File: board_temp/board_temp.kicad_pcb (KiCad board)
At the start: 2 copper layers, 4 parts, among them J1 Conn_02x16_Odd_Even, J2 Battery input, U1 BQ24074RGT, U2 INA219AxDCN

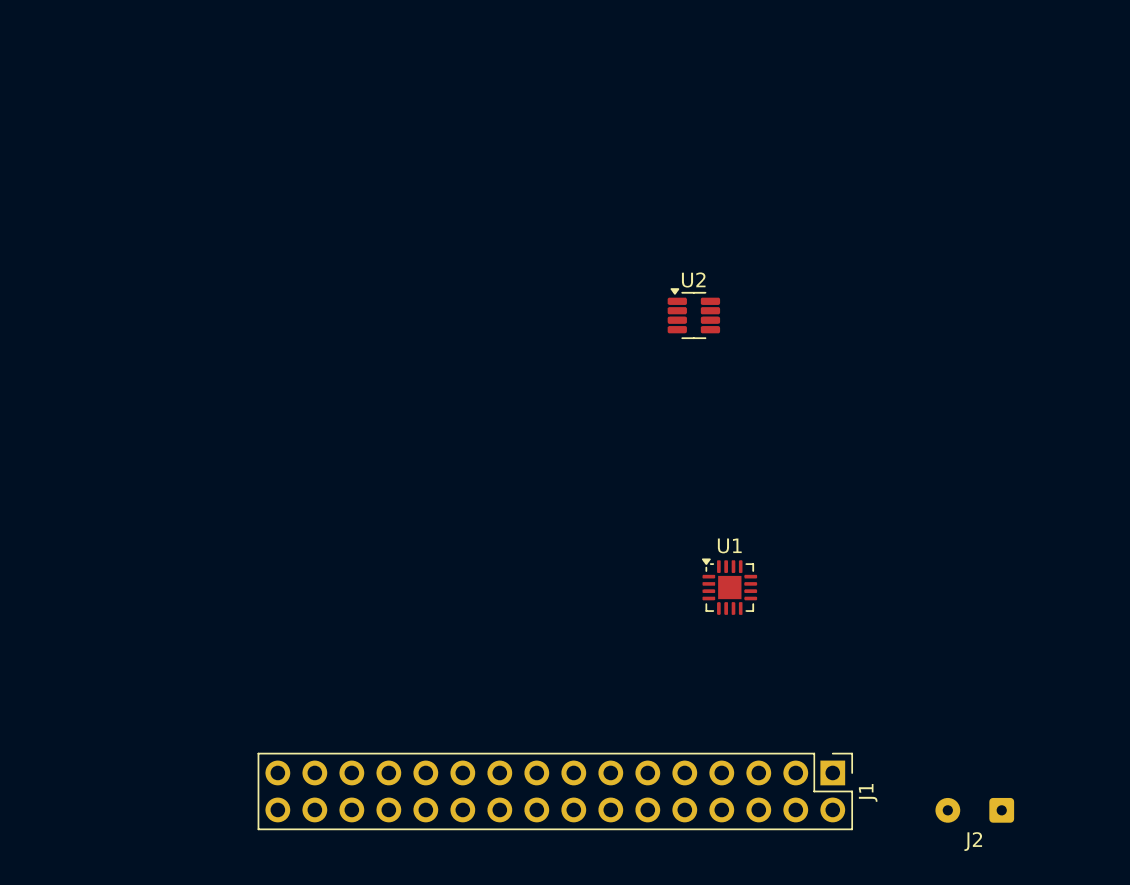
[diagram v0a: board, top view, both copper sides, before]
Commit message: changed charging config
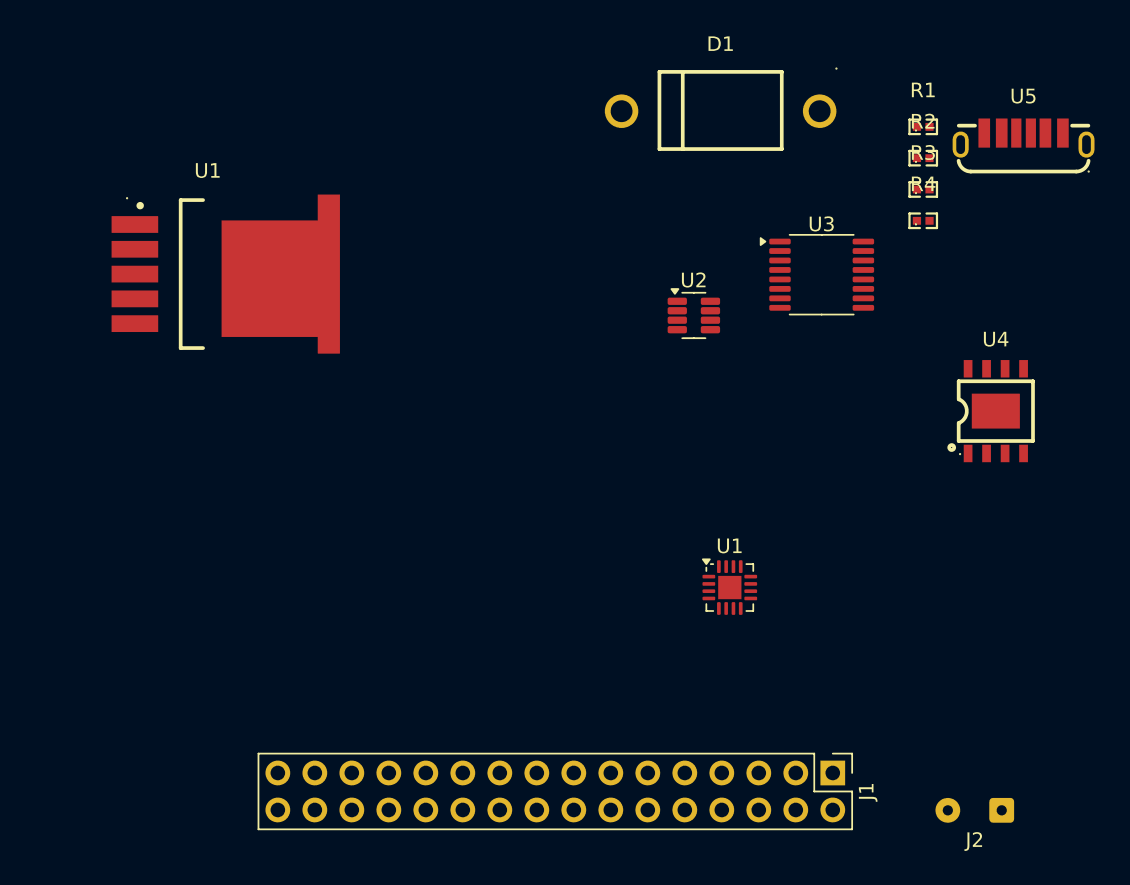
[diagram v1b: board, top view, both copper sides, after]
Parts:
- added D1: 1N5824_C7503125, xxcustom_footprint:DO-27_BD5.3-L8.4-P12.40-D1.3-RD, F.Cu at (161.7, 72.5)
- added R1: 2k, xxcustom_footprint:R0402, F.Cu at (175.6, 73.6)
- added R2: 2k, xxcustom_footprint:R0402, F.Cu at (175.6, 75.7)
- added R3: 1k, xxcustom_footprint:R0402, F.Cu at (175.6, 77.9)
- added R4: 1k, xxcustom_footprint:R0402, F.Cu at (175.6, 80.0)
- added U1: LM2596SX-5_0/NOPB, xxcustom_footprint:TO-263-5_L10.2-W8.9-P1.70-TL, F.Cu at (126.5, 83.7)
- added U3: IP2721, Package_SO:TSSOP-16_4.4x5mm_P0.65mm, F.Cu at (168.6, 83.7)
- added U4: TP4056_C382139, xxcustom_footprint:ESOP-8_L4.9-W3.9-P1.27-LS6.0-BL-EP, F.Cu at (180.6, 93.1)
- added U5: TYPE-C_6P_LTH6_5, xxcustom_footprint:USB-TYPE-C-SMD_TYPE-C-6P-LTH6.5, F.Cu at (182.5, 74.4)
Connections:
- U1 pad 14: unconnected-(U1-TMR-Pad14) -> GND
- U1 pad 4: unconnected-(U1-~{CE}-Pad4) -> GND
- U1 pad 5: unconnected-(U1-EN2-Pad5) -> 4.4V
- U1 pad 6: unconnected-(U1-EN1-Pad6) -> GND
- U2 pad 2: unconnected-(U2-IN--Pad2) -> Net-(U2-IN-)

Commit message: added USB PD
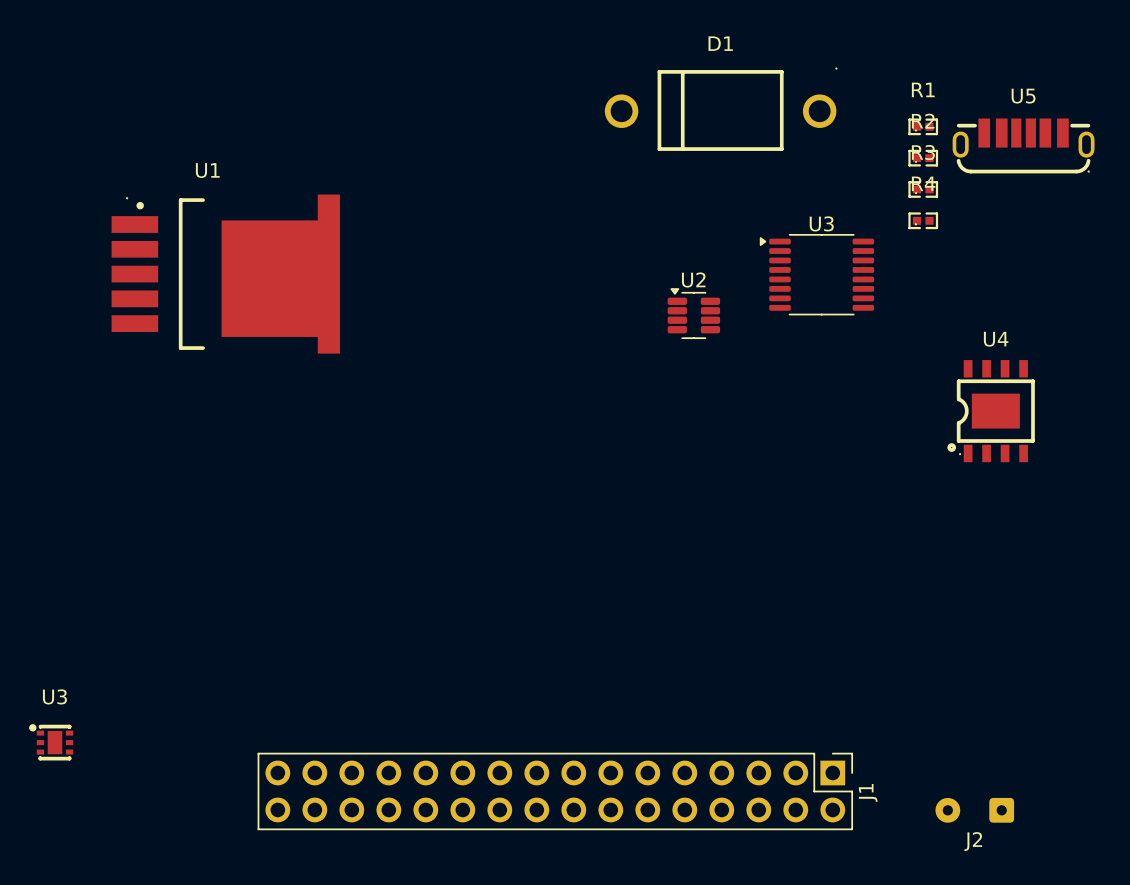
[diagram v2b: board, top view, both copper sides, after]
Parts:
- removed the U1 at (162.3, 105.2)
- added U3: HUSB237-AA001-DN06R, xxcustom_footprint:TDFN-6_L2.0-W2.0-P0.65-TL-EP, F.Cu at (116.0, 115.9)
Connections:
- net /Charge renamed /Charge+
- D1 pad 1: unconnected-(D1-K-Pad1) -> Net-(D1-K)
- D1 pad 2: unconnected-(D1-A-Pad2) -> GND
- J1 pad 22: 9V_ext -> 9V
- J1 pad 9: unconnected-(J1-Pin_9-Pad9) -> 9V
- U1 pad 1: unconnected-(U1-VIN-Pad1) -> 9V
- U1 pad 2: unconnected-(U1-OUTPUT-Pad2) -> Net-(D1-K)
- U1 pad 3: unconnected-(U1-GND-Pad3) -> GND
- U1 pad 4: unconnected-(U1-FB-Pad4) -> Buck_22
- U1 pad 5: unconnected-(U1-ON#/OFF-Pad5) -> GND
- U1 pad 6: unconnected-(U1-GND-Pad6) -> GND
- U2 pad 7: unconnected-(U2-A0-Pad7) -> /I2C1_SCL
- U2 pad 8: unconnected-(U2-A1-Pad8) -> /I2C1_SDA

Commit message: began schematic rev 3.0
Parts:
- removed D1: 1N5824_C7503125, xxcustom_footprint:DO-27_BD5.3-L8.4-P12.40-D1.3-RD
- added D2: SS34_C8678, xxcustom_footprint:SMA_L4.3-W2.6-LS5.2-RD, F.Cu at (165.0, 96.2)
- added J4: Conn_01x02, Connector_JST:JST_PH_S2B-PH-K_1x02_P2.00mm_Horizontal, F.Cu at (180.1, 106.7)
- added R8: 2k, xxcustom_footprint:R0402, F.Cu at (186.6, 105.4)
- added R9: 6k, xxcustom_footprint:R0402, F.Cu at (186.6, 107.5)
- added U6: SN74LVC1G3157DCKR, xxcustom_footprint:SC-70-6_L2.2-W1.3-P0.65-LS2.1-BR, F.Cu at (170.5, 105.5)
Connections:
- net +3.3V renamed /Vin
- net /Bat+ renamed Net-(U2-IN+)
- J1 pad 13: unconnected-(J1-Pin_13-Pad13) -> /fast_charge
- J1 pad 9: 9V -> unconnected-(J1-Pin_9-Pad9)
- U3 pad 1: unconnected-(U3-CC1-Pad1) -> Net-(J3-CC1)
- U3 pad 2: unconnected-(U3-VUSB-Pad2) -> 9V
- U3 pad 3: unconnected-(U3-VSET-Pad3) -> Net-(U3-VSET)
- U3 pad 6: unconnected-(U3-CC2-Pad6) -> Net-(J3-CC2)
- U3 pad 7: unconnected-(U3-GND-Pad7) -> GND
- U4 pad 2: Net-(U4-PROG) -> /R_prog
